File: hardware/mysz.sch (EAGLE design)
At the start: 21 parts, among them IC1 LM1117T(H)-3.3, U1 NUCLEO-L053R8

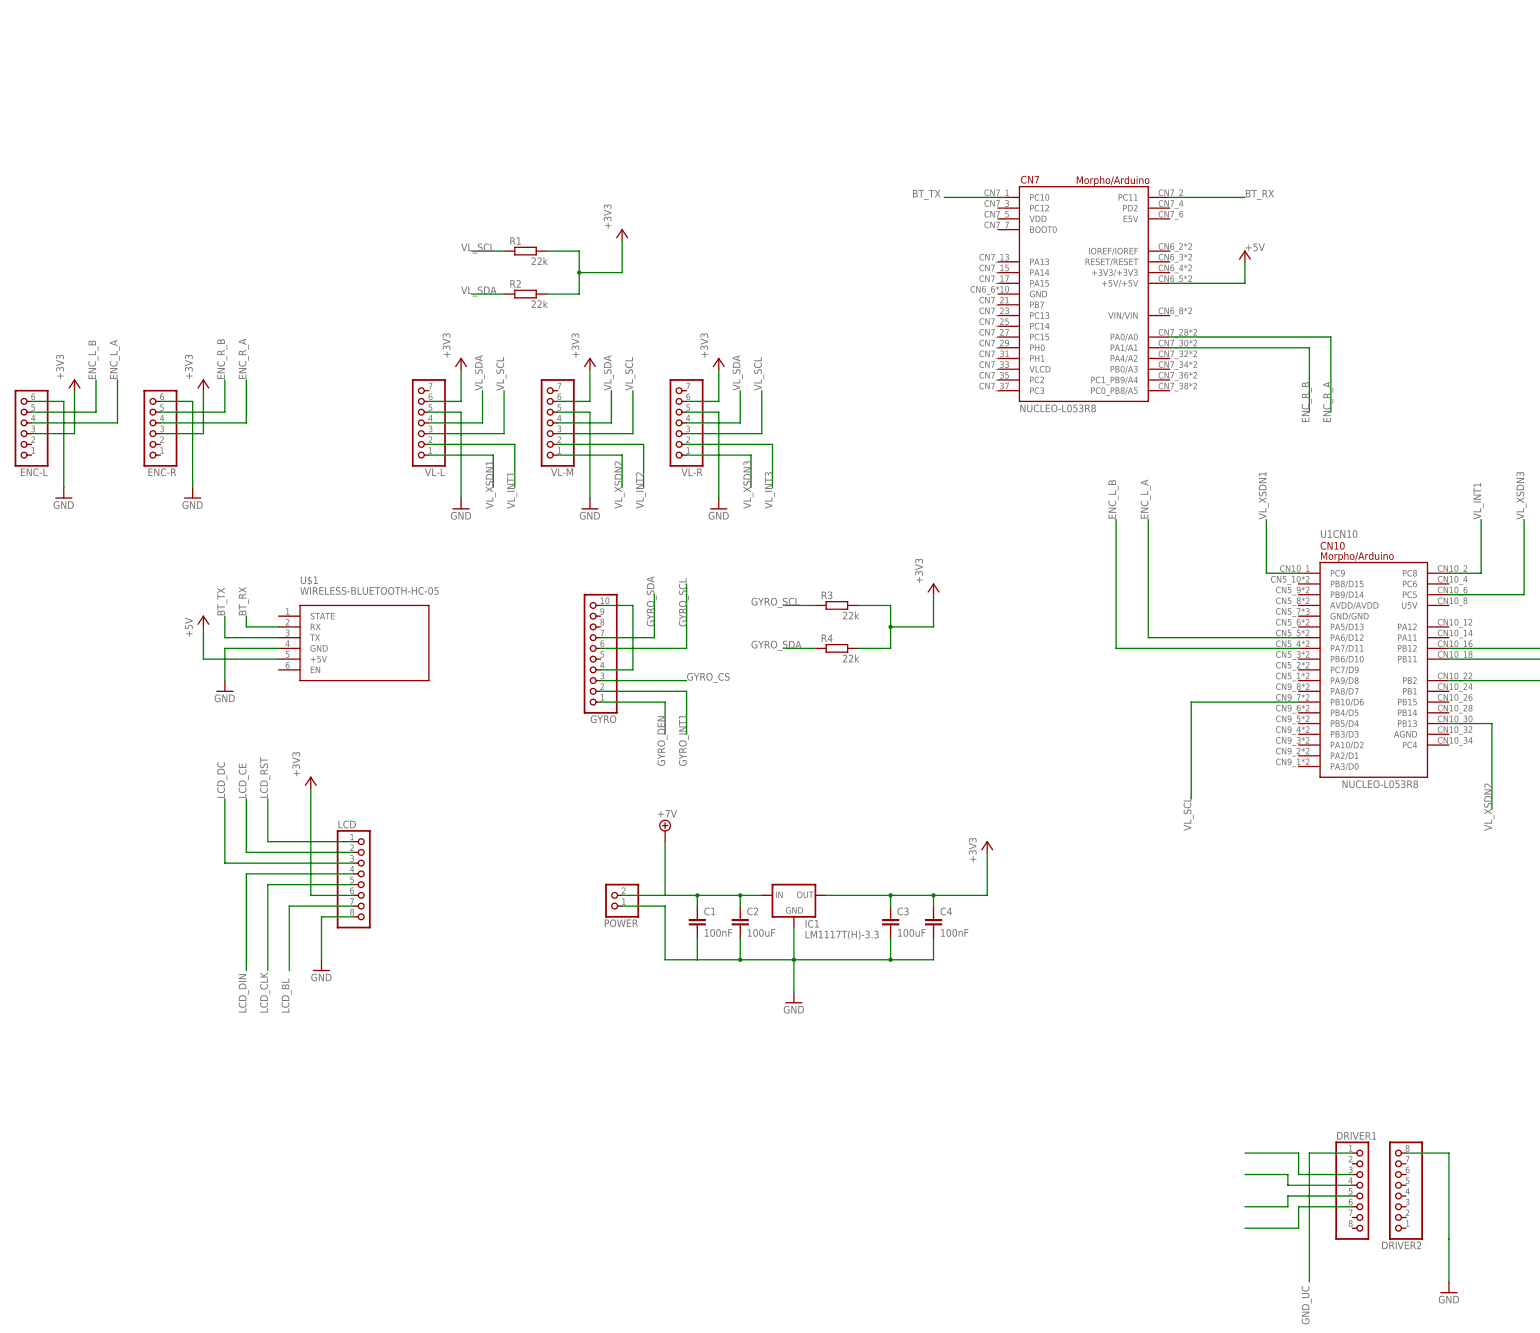
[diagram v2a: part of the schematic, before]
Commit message: conection models to stm & stm corected
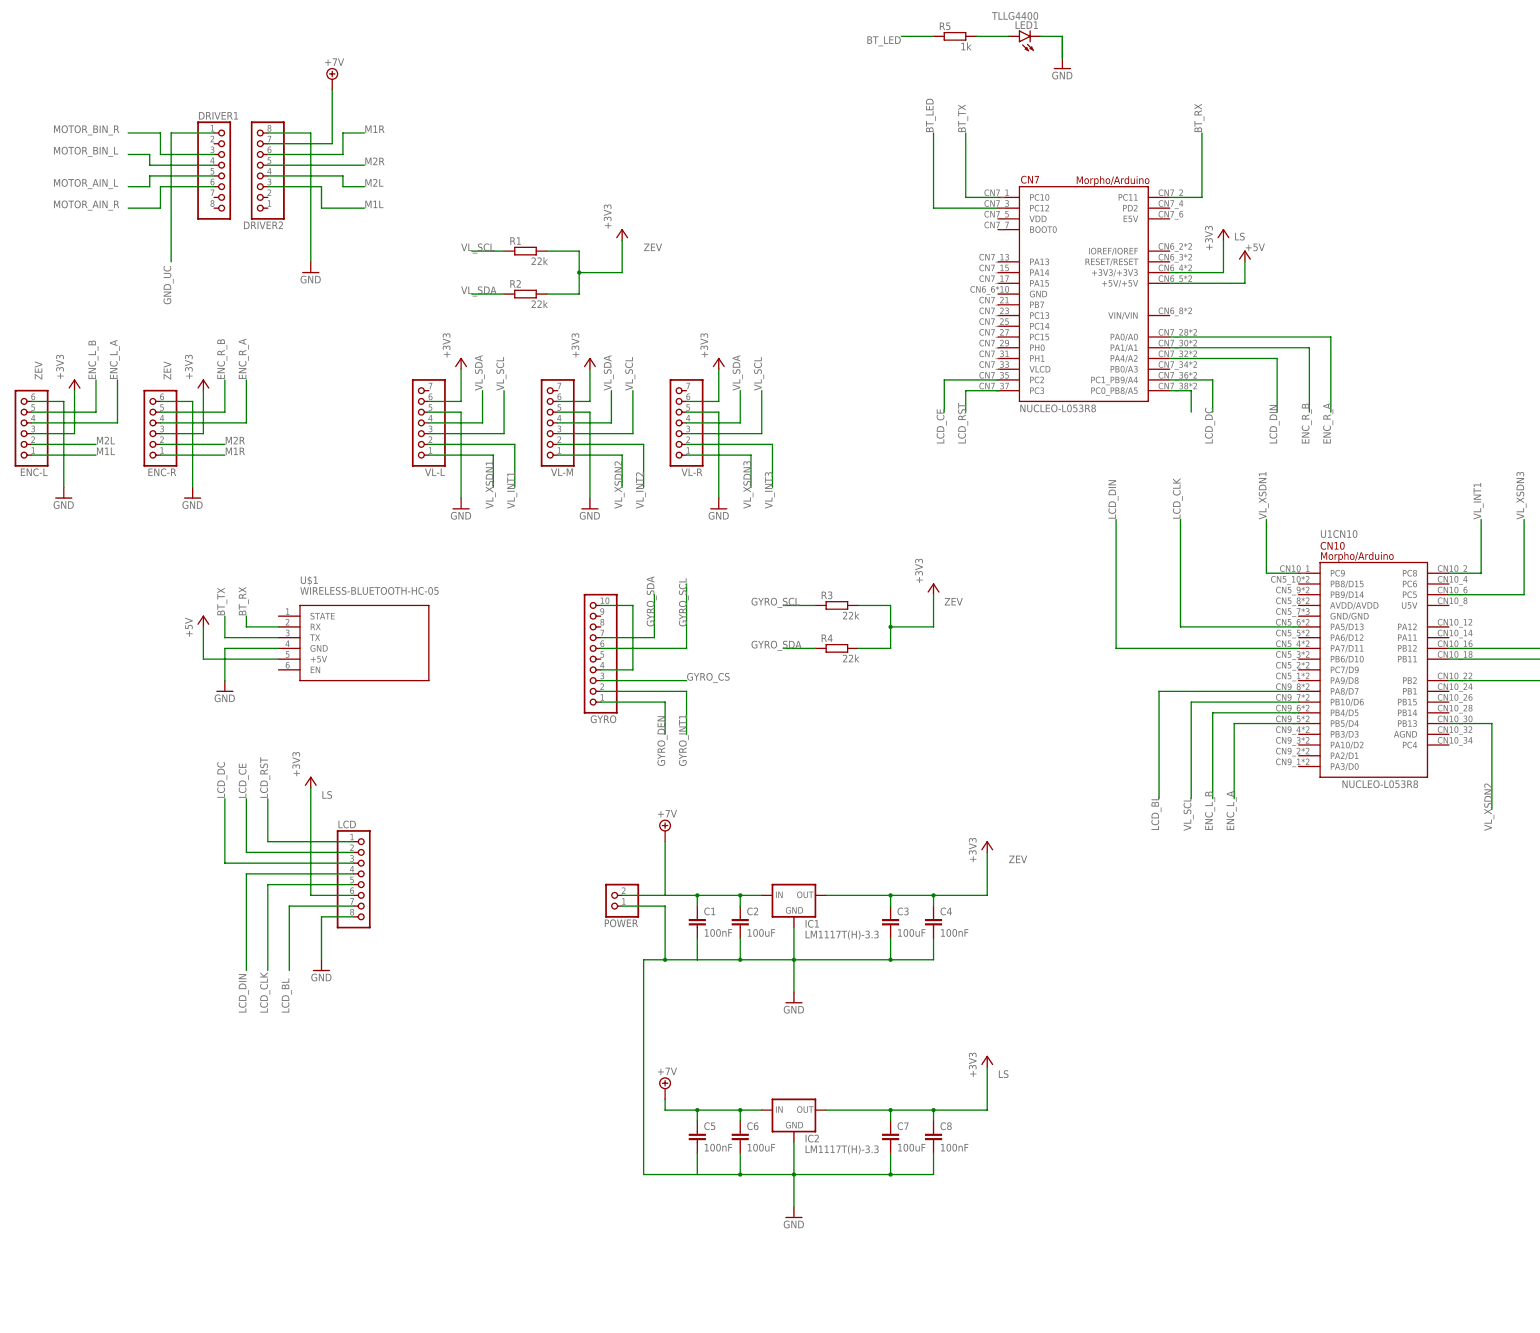
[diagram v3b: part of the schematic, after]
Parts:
- added C5, C8: 100nF, capacitor-wima:C2,5-3
- added C6, C7: 100uF, capacitor-wima:C2,5-3
- added IC2: LM1117T(H)-3.3, lm1117_10:LM1117T(H)-3.3
- added LED1: TLLG4400, led:TLLG4400
- added R5: 1k, rcl:R-EU_0207/10
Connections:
- net N$1 renamed MOTOR_BIN_R
- net N$2 renamed MOTOR_BIN_L
- net N$3 renamed MOTOR_AIN_L
- net N$5 renamed MOTOR_AIN_R
- new net BT_LED: R5.1, U1CN7.PC12
- new net LS: C7.1, C8.1, IC2.OUT, LCD.6, U1CN7.+3V3/+3V3
- new net M1L: DRIVER2.3, ENC-L.1
- new net M1R: DRIVER2.6, ENC-R.1
- new net M2L: DRIVER2.4, ENC-L.2
- new net M2R: DRIVER2.5, ENC-R.2
- new net N$1: LED1.C
- new net N$2: U1CN7.PC0_PB8/A5
- new net N$5: LED1.A, R5.2
- new net N$6: DRIVER2.7
- new net ZEV: C3.1, C4.1, ENC-L.3, ENC-R.3, IC1.OUT, R1.2, R2.2, R3.2, R4.2
- net +3V3: no longer C3.1, C4.1, ENC-L.3, ENC-R.3, IC1.OUT, LCD.6, R1.2, R2.2, R3.2, R4.2
- net +7V: now also C5.1, C6.1, IC2.IN
- net ENC_L_A: now also U1CN10.PB5/D4; no longer U1CN10.PA6/D12
- net ENC_L_B: now also U1CN10.PB4/D5; no longer U1CN10.PA7/D11
- net GND: now also C5.2, C6.2, C7.2, C8.2, IC2.GND
- net LCD_BL: now also U1CN10.PA8/D7
- net LCD_CE: now also U1CN7.PC2
- net LCD_CLK: now also U1CN10.PA5/D13
- net LCD_DC: now also U1CN7.PC1_PB9/A4
- net LCD_DIN: now also U1CN10.PA7/D11, U1CN7.PA4/A2
- net LCD_RST: now also U1CN7.PC3
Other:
- moved on the sheet: DRIVER1, DRIVER2

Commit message: finished hardware & stm I2C problem
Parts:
- added C11: 100nF, rcl:C-EUC0402
- added S2: DTSM-3, dtsm3:DTSM-3
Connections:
- new net BUTTON1: C11.1, S2.2
- net GND_UC: now also U1CN10.GND/GND
- net MOTOR_AIN_L: now also U1CN10.PB1
- net MOTOR_AIN_R: now also U1CN10.PA9/D8
- net MOTOR_BIN_L: now also U1CN7.PB0/A3
- net MOTOR_BIN_R: now also U1CN10.PA10/D2
- net N$1: now also C11.2, S2.1

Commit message: WDS init & schem finished
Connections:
- removed net GYRO_CS: GYRO.3
- removed net N$2: U1CN7.PC0_PB8/A5
- removed net N$4: GYRO.10, GYRO.4
- net BUTTON1: now also U1CN10.PC6
- net ENC_L_A: now also U1CN10.PB4/D5; no longer U1CN10.PB5/D4
- net ENC_L_B: now also U1CN10.PB5/D4; no longer U1CN10.PB4/D5
- net GYRO_DEN: now also U1CN10.PA11
- net GYRO_INT1: now also U1CN10.PA12
- net GYRO_SCL: now also U1CN10.PB6/D10
- net GYRO_SDA: now also U1CN7.PB7
- net VL_INT2: now also U1CN10.PC4; no longer U1CN10.PB12
- net ZEV: now also GYRO.10, GYRO.3, GYRO.4
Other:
- moved on the sheet: R3, R4

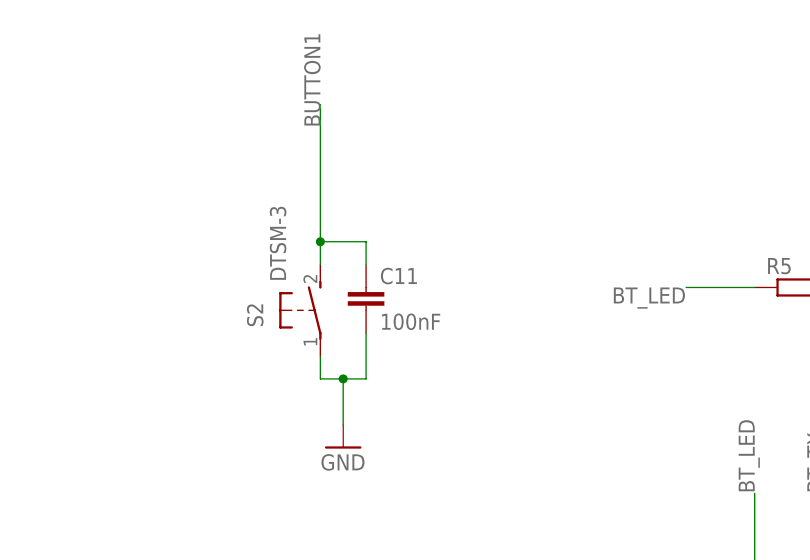
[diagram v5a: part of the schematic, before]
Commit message: switched capacitor
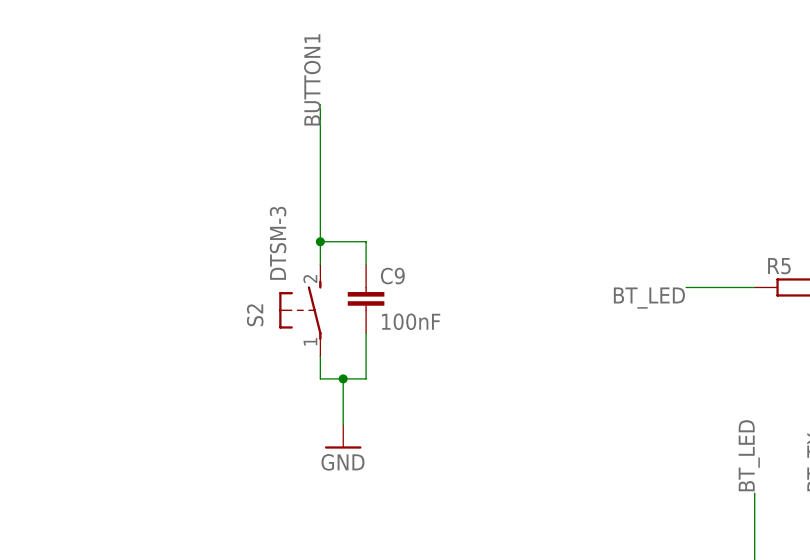
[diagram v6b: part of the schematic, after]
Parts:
- removed C11: 100nF, rcl:C-EUC0402
- added C9: 100nF, capacitor-wima:C2,5-3
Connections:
- net BUTTON1: now also C9.1; no longer C11.1
- net N$1: now also C9.2; no longer C11.2
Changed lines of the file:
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@@
 <part name="GND11" library="supply1" library_urn="urn:adsk.eagle:library:371" deviceset="GND" device=""/>
 <part name="S2" library="dtsm3" deviceset="DTSM-3" device=""/>
-<part name="C11" library="rcl" deviceset="C-EU" device="C0402" value="100nF"/>
 <part name="GND12" library="supply1" library_urn="urn:adsk.eagle:library:371" deviceset="GND" device=""/>
 <part name="+3V12" library="supply1" library_urn="urn:adsk.eagle:library:371" deviceset="+3V3" device=""/>
 <part name="+3V13" library="supply1" library_urn="urn:adsk.eagle:library:371" deviceset="+3V3" device=""/>
+<part name="C9" library="capacitor-wima" library_urn="urn:adsk.eagle:library:116" deviceset="C" device="2,5-3" package3d_urn="urn:adsk.eagle:package:5436/1" value="100nF"/>
 </parts>
 <sheets>
@@
 <attribute name="VALUE" x="130.81" y="165.735" size="1.778" layer="96" rot="R90"/>
 </instance>
-<instance part="C11" gate="G$1" x="139.7" y="165.1" smashed="yes">
+<instance part="GND12" gate="1" x="137.16" y="147.32" smashed="yes">
+<attribute name="VALUE" x="134.62" y="144.78" size="1.778" layer="96"/>
+</instance>
+<instance part="+3V12" gate="G$1" x="111.76" y="43.18" smashed="yes">
+<attribute name="VALUE" x="109.22" y="43.18" size="1.778" layer="96" rot="R90"/>
+</instance>
+<instance part="+3V13" gate="G$1" x="132.08" y="27.94" smashed="yes">
+<attribute name="VALUE" x="129.54" y="27.94" size="1.778" layer="96" rot="R90"/>
+</instance>
+<instance part="C9" gate="G$1" x="139.7" y="165.1" smashed="yes">
 <attribute name="NAME" x="141.224" y="165.481" size="1.778" layer="95"/>
 <attribute name="VALUE" x="141.224" y="160.401" size="1.778" layer="96"/>
-</instance>
-<instance part="GND12" gate="1" x="137.16" y="147.32" smashed="yes">
-<attribute name="VALUE" x="134.62" y="144.78" size="1.778" layer="96"/>
-</instance>
-<instance part="+3V12" gate="G$1" x="111.76" y="43.18" smashed="yes">
-<attribute name="VALUE" x="109.22" y="43.18" size="1.778" layer="96" rot="R90"/>
-</instance>
-<instance part="+3V13" gate="G$1" x="132.08" y="27.94" smashed="yes">
-<attribute name="VALUE" x="129.54" y="27.94" size="1.778" layer="96" rot="R90"/>
 </instance>
 </instances>
@@
 <pinref part="S2" gate="G$1" pin="1"/>
 <wire x1="134.62" y1="157.48" x2="134.62" y2="154.94" width="0.1524" layer="91"/>
-<pinref part="C11" gate="G$1" pin="2"/>
 <wire x1="134.62" y1="154.94" x2="137.16" y2="154.94" width="0.1524" layer="91"/>
 <wire x1="137.16" y1="154.94" x2="139.7" y2="154.94" width="0.1524" layer="91"/>
 <wire x1="139.7" y1="154.94" x2="139.7" y2="160.02" width="0.1524" layer="91"/>
 <junction x="137.16" y="154.94"/>
+<pinref part="C9" gate="G$1" pin="2"/>
 </segment>
 </net>
@@
 <wire x1="134.62" y1="167.64" x2="134.62" y2="170.18" width="0.1524" layer="91"/>
 <label x="134.62" y="182.88" size="1.778" layer="95" rot="R90"/>
-<pinref part="C11" gate="G$1" pin="1"/>
 <wire x1="134.62" y1="170.18" x2="134.62" y2="185.42" width="0.1524" layer="91"/>
 <wire x1="134.62" y1="170.18" x2="139.7" y2="170.18" width="0.1524" layer="91"/>
 <wire x1="139.7" y1="170.18" x2="139.7" y2="167.64" width="0.1524" layer="91"/>
 <junction x="134.62" y="170.18"/>
-</segment>
-<segment>
+<pinref part="C9" gate="G$1" pin="1"/>
+</segment>
+<segment>
